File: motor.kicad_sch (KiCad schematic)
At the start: 15 parts, among them J1 Conn_02x06_Top_Bottom, J2 Conn_02x06_Top_Bottom, J3 Conn_02x06_Top_Bottom, J4 Conn_02x06_Top_Bottom, J5 Conn_02x06_Top_Bottom, J6 Conn_02x06_Top_Bottom, M7 MOTOR, M8 MOTOR, M9 MOTOR, U10 SINGLETB9051FTG_MOTOR_DRIVER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

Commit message: Schematic Overhaul
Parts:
- removed J1, J2, J3, J4, J5, J6: Conn_02x06_Top_Bottom, symbol Connector_Generic:Conn_02x06_Top_Bottom
- removed M7, M8, M9: MOTOR, MOTOR:VIBE-MOTOR-10MM, symbol ME3230:MOTOR
- removed U10, U4, U8: SINGLETB9051FTG_MOTOR_DRIVER, SINGLETB9051FTG_MOTOR_DRIVER:SINGLETB9051FTG, symbol ME3230:SINGLETB9051FTG_MOTOR_DRIVER
- removed U11, U5, U9: ENCODER, ENCODER:ENCODER, symbol ME3230:ENCODER
- added J1, J2, J3: Conn_02x06_Row_Letter_Last, symbol Connector_Generic:Conn_02x06_Row_Letter_Last
- added J4: Screw_Terminal_01x02, symbol Connector:Screw_Terminal_01x02
- added J5: Conn_02x18_Row_Letter_Last, symbol Connector_Generic:Conn_02x18_Row_Letter_Last
- added U1, U2, U3: SINGLETB9051FTG_MOTOR_DRIVER, SINGLETB9051FTG_MOTOR_DRIVER:SINGLETB9051FTG, symbol ME3230:SINGLETB9051FTG_MOTOR_DRIVER
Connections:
- new net: J1.5a (Pin_5a), U1.P13 (OUT2)
- new net: J1.6a (Pin_6a), U1.P14 (OUT1)
- new net: J2.5a (Pin_5a), U2.P13 (OUT2)
- new net: J2.6a (Pin_6a), U2.P14 (OUT1)
- new net: J3.5a (Pin_5a), U3.P13 (OUT2)
- new net: J3.6a (Pin_6a), U3.P14 (OUT1)
- new net 9.6V: J4.2 (Pin_2), U1.P11 (VIN), U2.P11 (VIN), U3.P11 (VIN)
- new net Ard1: J5.1b (Pin_1b), U1.P2 (EN)
- new net Ard10: J5.10b (Pin_10b), U2.P9 (OCM)
- new net Ard11: J2.2a (Pin_2a), J5.11b (Pin_11b)
- new net Ard12: J2.1a (Pin_1a), J5.12b (Pin_12b)
- new net Ard13: J5.13b (Pin_13b), U3.P2 (EN)
- new net Ard14: J5.14b (Pin_14b), U3.P7 (PWM2)
- new net Ard15: J5.15b (Pin_15b), U3.P8 (PWM1)
- new net Ard16: J5.16b (Pin_16b), U3.P9 (OCM)
- new net Ard17: J3.2a (Pin_2a), J5.17b (Pin_17b)
- new net Ard18: J3.1a (Pin_1a), J5.18b (Pin_18b)
- new net Ard2: J5.2b (Pin_2b), U1.P7 (PWM2)
- new net Ard3: J5.3b (Pin_3b), U1.P8 (PWM1)
- new net Ard4: J5.4b (Pin_4b), U1.P9 (OCM)
- new net Ard5: J1.2a (Pin_2a), J5.5b (Pin_5b)
- new net Ard6: J1.1a (Pin_1a), J5.6b (Pin_6b)
- new net Ard7: J5.7b (Pin_7b), U2.P2 (EN)
- new net Ard8: J5.8b (Pin_8b), U2.P7 (PWM2)
- new net Ard9: J5.9b (Pin_9b), U2.P8 (PWM1)
- new net Can be 9V or 5V: J1.3a (Pin_3a), J2.3a (Pin_3a), J3.3a (Pin_3a)
- new net GND: J1.4a (Pin_4a), J2.4a (Pin_4a), J3.4a (Pin_4a), J4.1 (Pin_1), U1.P5 (GND), U2.P5 (GND), U3.P5 (GND)
- new net M1_1: J1.1b (Pin_1b)
- new net M1_2: J1.2b (Pin_2b)
- new net M1_3: J1.3b (Pin_3b)
- new net M1_4: J1.4b (Pin_4b)
- new net M1_5: J1.5b (Pin_5b)
- new net M1_6: J1.6b (Pin_6b)
- new net M2_1: J2.1b (Pin_1b)
- new net M2_2: J2.2b (Pin_2b)
- new net M2_3: J2.3b (Pin_3b)
- new net M2_4: J2.4b (Pin_4b)
- new net M2_5: J2.5b (Pin_5b)
- new net M2_6: J2.6b (Pin_6b)
- new net M3_1: J3.1b (Pin_1b)
- new net M3_2: J3.2b (Pin_2b)
- new net M3_3: J3.3b (Pin_3b)
- new net M3_4: J3.4b (Pin_4b)
- new net M3_5: J3.5b (Pin_5b)
- new net M3_6: J3.6b (Pin_6b)
- new net MC1: J5.1a (Pin_1a)
- new net MC10: J5.10a (Pin_10a)
- new net MC11: J5.11a (Pin_11a)
- new net MC12: J5.12a (Pin_12a)
- new net MC13: J5.13a (Pin_13a)
- new net MC14: J5.14a (Pin_14a)
- new net MC15: J5.15a (Pin_15a)
- new net MC16: J5.16a (Pin_16a)
- new net MC17: J5.17a (Pin_17a)
- new net MC18: J5.18a (Pin_18a)
- new net MC2: J5.2a (Pin_2a)
- new net MC3: J5.3a (Pin_3a)
- new net MC4: J5.4a (Pin_4a)
- new net MC5: J5.5a (Pin_5a)
- new net MC6: J5.6a (Pin_6a)
- new net MC7: J5.7a (Pin_7a)
- new net MC8: J5.8a (Pin_8a)
- new net MC9: J5.9a (Pin_9a)
- new net VCC: U1.P1 (ENB), U1.P3 (OCC), U1.P4 (VCC), U2.P1 (ENB), U2.P3 (OCC), U2.P4 (VCC), U3.P1 (ENB), U3.P3 (OCC), U3.P4 (VCC)
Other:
- note added: "Black"
- note added: "Blue"
- note added: "Green"
- note added: "Red"
- note added: "White"
- note added: "Yellow"
- note removed: "Logic Power from Buck"
- note removed: "Power from Battery"
- note removed: "data pins to arduino"
- title: (none) -> Motor Controller Proto-Board

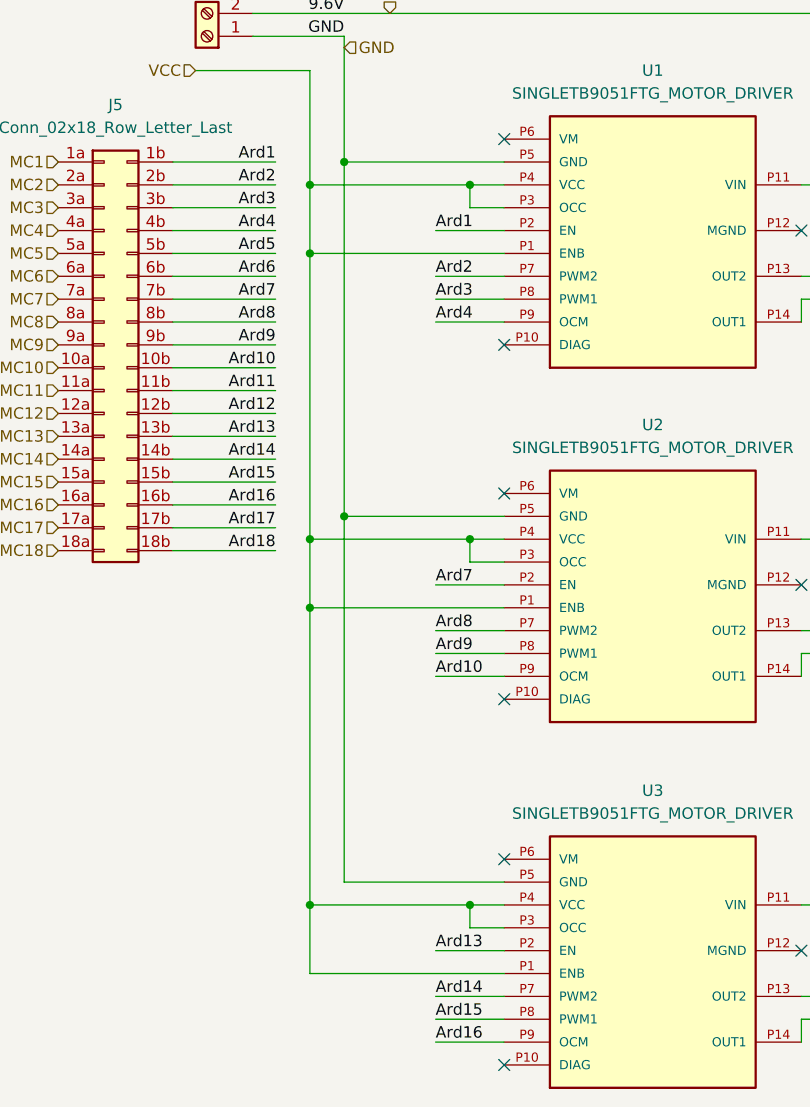
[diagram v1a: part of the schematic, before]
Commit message: Fixed ENB jumper
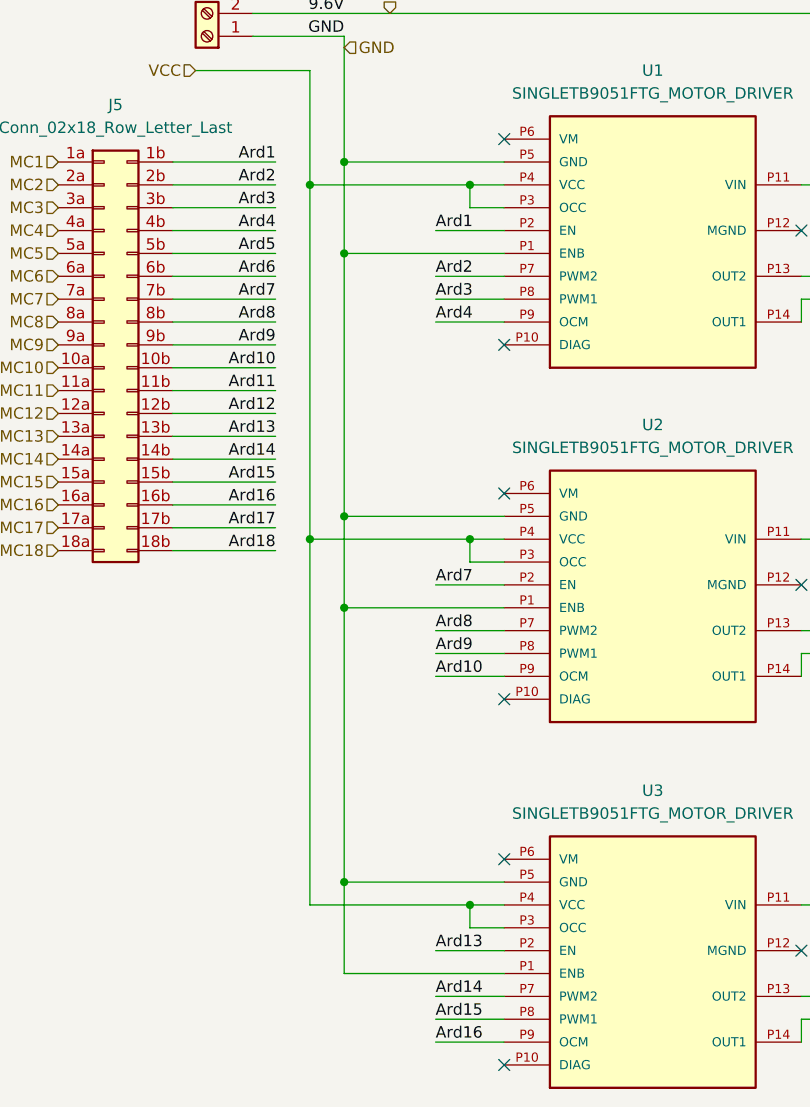
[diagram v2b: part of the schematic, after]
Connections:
- net GND: now also U1.P1 (ENB), U2.P1 (ENB), U3.P1 (ENB)
- net VCC: no longer U1.P1 (ENB), U2.P1 (ENB), U3.P1 (ENB)
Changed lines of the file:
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@@
+	)
+	(junction
+		(at 59.69 85.09)
+		(diameter 0)
+		(color 0 0 0 0)
 	)
 	(junction
@@
 	)
 	(junction
-		(at 55.88 118.11)
-		(diameter 0)
-		(color 0 0 0 0)
-	)
-	(junction
-		(at 55.88 45.72)
-		(diameter 0)
-		(color 0 0 0 0)
-	)
-	(junction
 		(at 113.03 77.47)
 		(diameter 0)
@@
 	)
 	(junction
+		(at 59.69 115.57)
+		(diameter 0)
+		(color 0 0 0 0)
+	)
+	(junction
 		(at 148.59 85.09)
 		(diameter 0)
@@
 	)
 	(junction
-		(at 55.88 85.09)
+		(at 59.69 45.72)
 		(diameter 0)
 		(color 0 0 0 0)
@@
 	(wire
 		(pts
-			(xy 55.88 125.73) (xy 55.88 118.11)
-		)
-		(stroke
-			(width 0)
-			(type default)
-		)
-	)
-	(wire
-		(pts
 			(xy 158.75 40.64) (xy 143.51 40.64)
 		)
@@
 	(wire
 		(pts
-			(xy 55.88 38.1) (xy 55.88 45.72)
-		)
-		(stroke
-			(width 0)
-			(type default)
-		)
-	)
-	(wire
-		(pts
 			(xy 121.92 80.01) (xy 130.81 80.01)
 		)
@@
 	(wire
 		(pts
-			(xy 55.88 118.11) (xy 55.88 85.09)
+			(xy 55.88 77.47) (xy 55.88 118.11)
 		)
 		(stroke
@@
 	(wire
 		(pts
+			(xy 77.47 125.73) (xy 59.69 125.73)
+		)
+		(stroke
+			(width 0)
+			(type default)
+		)
+	)
+	(wire
+		(pts
 			(xy 69.85 133.35) (xy 77.47 133.35)
 		)
@@
 	(wire
 		(pts
-			(xy 55.88 85.09) (xy 55.88 77.47)
-		)
-		(stroke
-			(width 0)
-			(type default)
-		)
-	)
-	(wire
-		(pts
 			(xy 73.66 118.11) (xy 73.66 120.65)
 		)
@@
 	(wire
 		(pts
-			(xy 55.88 85.09) (xy 77.47 85.09)
-		)
-		(stroke
-			(width 0)
-			(type default)
-		)
-	)
-	(wire
-		(pts
 			(xy 40.64 71.12) (xy 52.07 71.12)
 		)
@@
 	(wire
 		(pts
+			(xy 59.69 85.09) (xy 77.47 85.09)
+		)
+		(stroke
+			(width 0)
+			(type default)
+		)
+	)
+	(wire
+		(pts
 			(xy 59.69 115.57) (xy 77.47 115.57)
 		)
@@
 	(wire
 		(pts
+			(xy 59.69 45.72) (xy 77.47 45.72)
+		)
+		(stroke
+			(width 0)
+			(type default)
+		)
+	)
+	(wire
+		(pts
 			(xy 113.03 77.47) (xy 110.49 77.47)
 		)
@@
 	(wire
 		(pts
-			(xy 59.69 35.56) (xy 59.69 74.93)
+			(xy 59.69 35.56) (xy 59.69 45.72)
 		)
 		(stroke
@@
 	(wire
 		(pts
-			(xy 55.88 45.72) (xy 55.88 77.47)
+			(xy 55.88 38.1) (xy 55.88 77.47)
 		)
 		(stroke
@@
 	(wire
 		(pts
+			(xy 59.69 85.09) (xy 59.69 115.57)
+		)
+		(stroke
+			(width 0)
+			(type default)
+		)
+	)
+	(wire
+		(pts
 			(xy 158.75 118.11) (xy 143.51 118.11)
 		)
@@
 	(wire
 		(pts
-			(xy 59.69 74.93) (xy 59.69 115.57)
+			(xy 59.69 74.93) (xy 59.69 85.09)
 		)
 		(stroke
@@
 	(wire
 		(pts
+			(xy 59.69 45.72) (xy 59.69 74.93)
+		)
+		(stroke
+			(width 0)
+			(type default)
+		)
+	)
+	(wire
+		(pts
 			(xy 151.13 123.19) (xy 143.51 123.19)
 		)
@@
 	(wire
 		(pts
+			(xy 59.69 125.73) (xy 59.69 115.57)
+		)
+		(stroke
+			(width 0)
+			(type default)
+		)
+	)
+	(wire
+		(pts
 			(xy 40.64 60.96) (xy 52.07 60.96)
 		)
@@
 	(wire
 		(pts
-			(xy 77.47 45.72) (xy 55.88 45.72)
-		)
-		(stroke
-			(width 0)
-			(type default)
-		)
-	)
-	(wire
-		(pts
 			(xy 73.66 80.01) (xy 73.66 77.47)
 		)
 		(stroke
-			(width 0)
-			(type default)
-		)
-	)
-	(wire
-		(pts
-			(xy 77.47 125.73) (xy 55.88 125.73)
-		)
-		(stroke
